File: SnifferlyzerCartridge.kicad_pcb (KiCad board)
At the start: 2 copper layers, 64.8 x 55.9 mm, 3 parts, among them J1 Cartridge Connector, U1 W25Q128

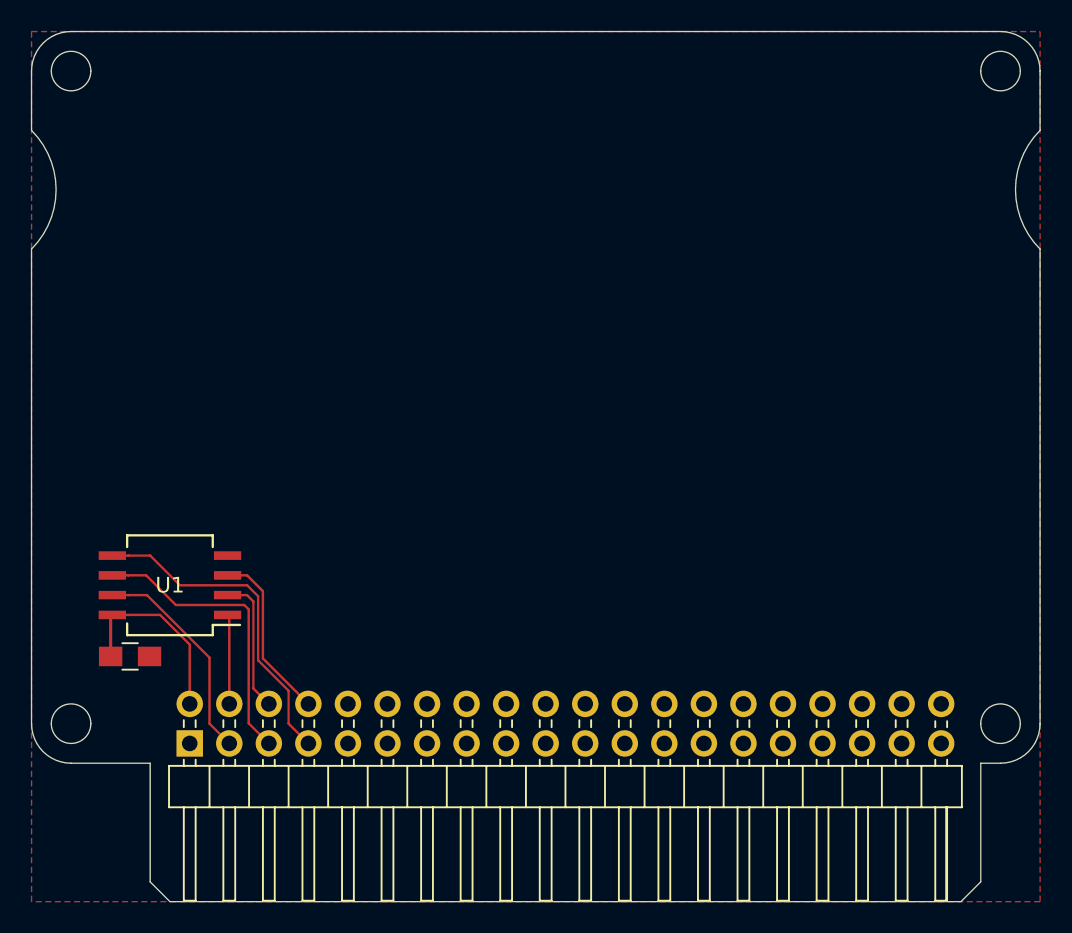
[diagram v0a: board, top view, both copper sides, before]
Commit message: First design of the Snifferlyzer cartridge
Also updated:
- README
- Render image
- .gitignore
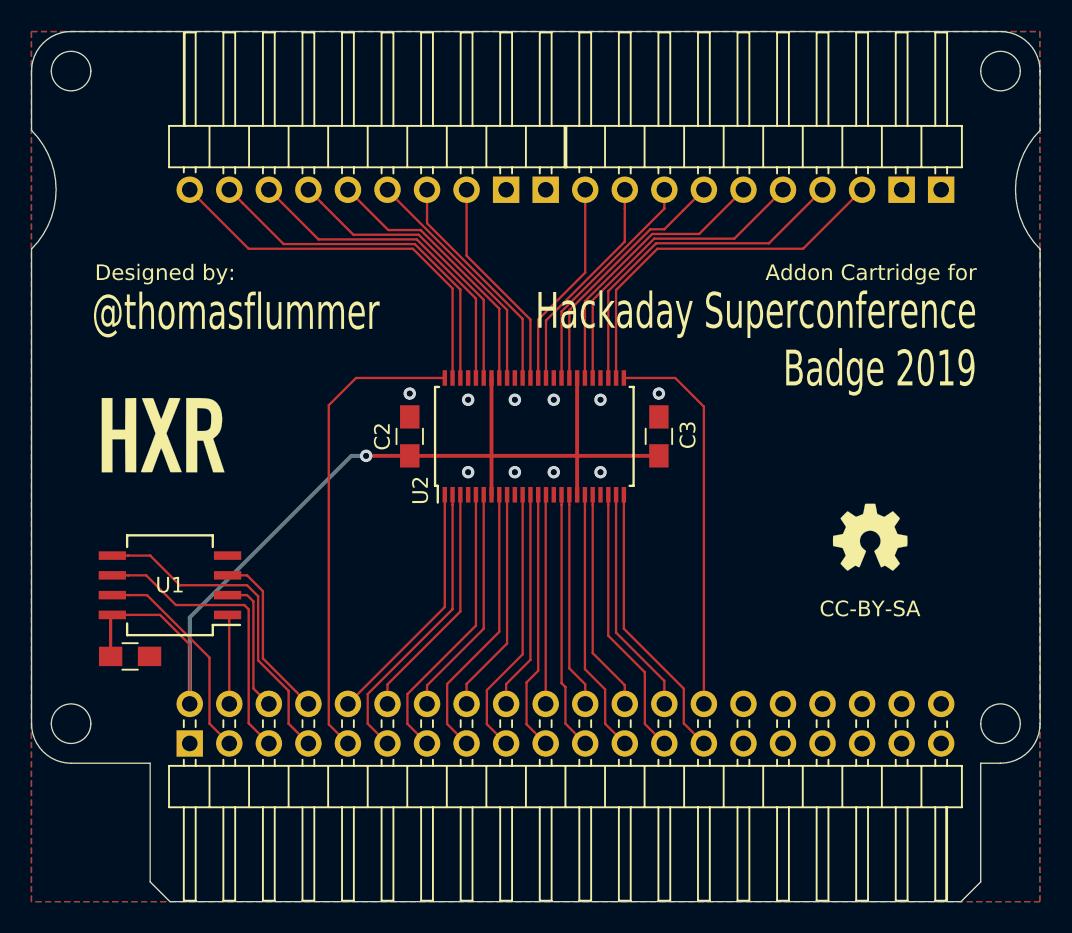
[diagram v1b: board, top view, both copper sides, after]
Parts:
- added C2: 100nF, Capacitors_SMD:C_0805_HandSoldering, F.Cu at (91.6, 76.8)
- added C3: 100nF, Capacitors_SMD:C_0805_HandSoldering, F.Cu at (107.6, 76.8)
- added G***: LOGO, Aesthetics:snifferlyzer_labels, B.Cu at (101.9, 55.4)
- added G***: LOGO, Aesthetics:oshw_logo_5.0mm, F.Cu at (121.2, 83.3)
- added G***: LOGO, Aesthetics:HXR_logo_small, F.Cu at (78.5, 76.7)
- added J2: Conn_01x10_Male, Pin_Headers:Pin_Header_Angled_1x10_Pitch2.54mm, F.Cu at (77.5, 61.0)
- added J3: Conn_01x10_Male, Pin_Headers:Pin_Header_Angled_1x10_Pitch2.54mm, F.Cu at (102.9, 61.0)
- added U2: 74LCX16245, Housings_SSOP:TSSOP-48_6.1x12.5mm_Pitch0.5mm, F.Cu at (99.6, 76.8)
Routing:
- net +3V3: track 12.3 -> 67.3 mm, vias 0 -> 1
- net GENIO1: track 0.00 -> 30.4 mm
- net IOA1: track 0.00 -> 25.3 mm
- net GENIO20: track 0.00 -> 25.0 mm
- net IOB8: track 0.00 -> 24.1 mm
- net IOA2: track 0.00 -> 23.2 mm
- net IOB7: track 0.00 -> 22.0 mm
- net IOA3: track 0.00 -> 21.3 mm
- net IOB6: track 0.00 -> 20.2 mm
- net IOA4: track 0.00 -> 19.2 mm
- net GENIO3: track 0.00 -> 18.8 mm
- net GENIO5: track 0.00 -> 18.3 mm
- net GENIO19: track 0.00 -> 18.1 mm
- net IOB5: track 0.00 -> 18.1 mm
- net GENIO7: track 0.00 -> 17.9 mm
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- added copper zone on B.Cu, net GND
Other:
- net class Default: clearance 0.2 -> 0.15
- rule trace_clearance: 0.2 -> 0.15
- rule trace_min: 0.2 -> 0.15
- board text added: "@thomasflummer"
- board text added: "Addon Cartridge for"
- board text added: "CC-BY-SA"
- board text added: "Designed by:"
- board text added: "Hackaday Superconference Badge 2019"
- board text added: "SNIFFERLYZER"
